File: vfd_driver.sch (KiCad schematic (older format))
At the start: 29 parts, among them J1 Input, J2 FIL, J3 HV, Q1 IRLZ34, U1 LM4871, U8 LM555

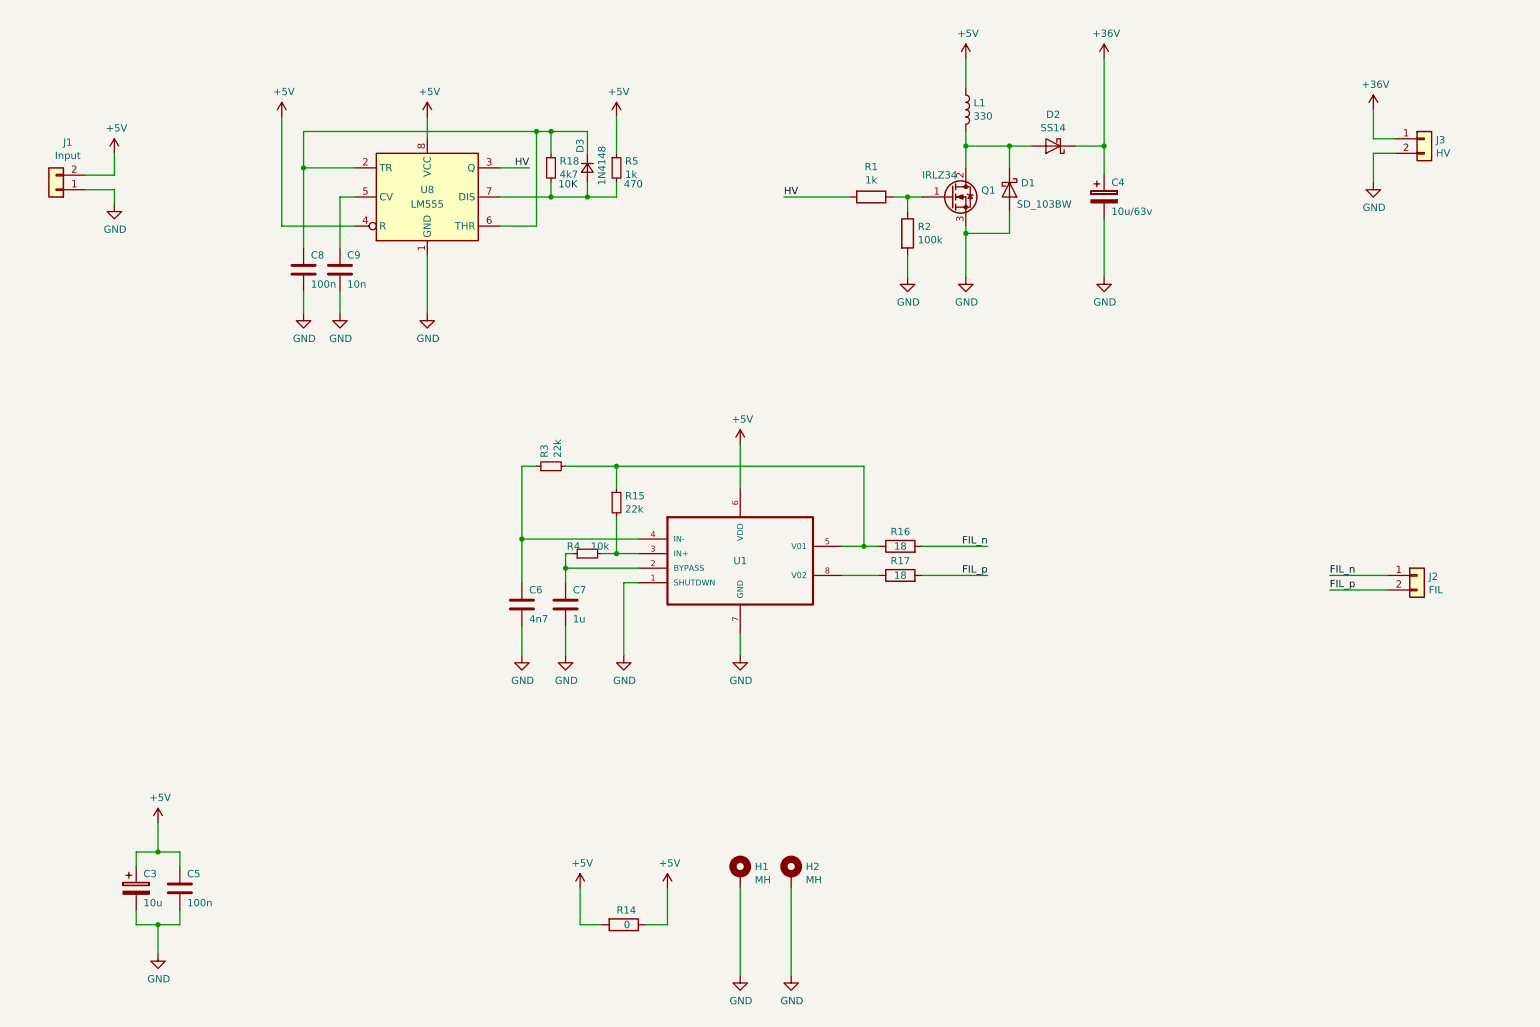
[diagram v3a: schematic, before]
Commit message: Separated input for the step up driver so ca be supply with 12V.
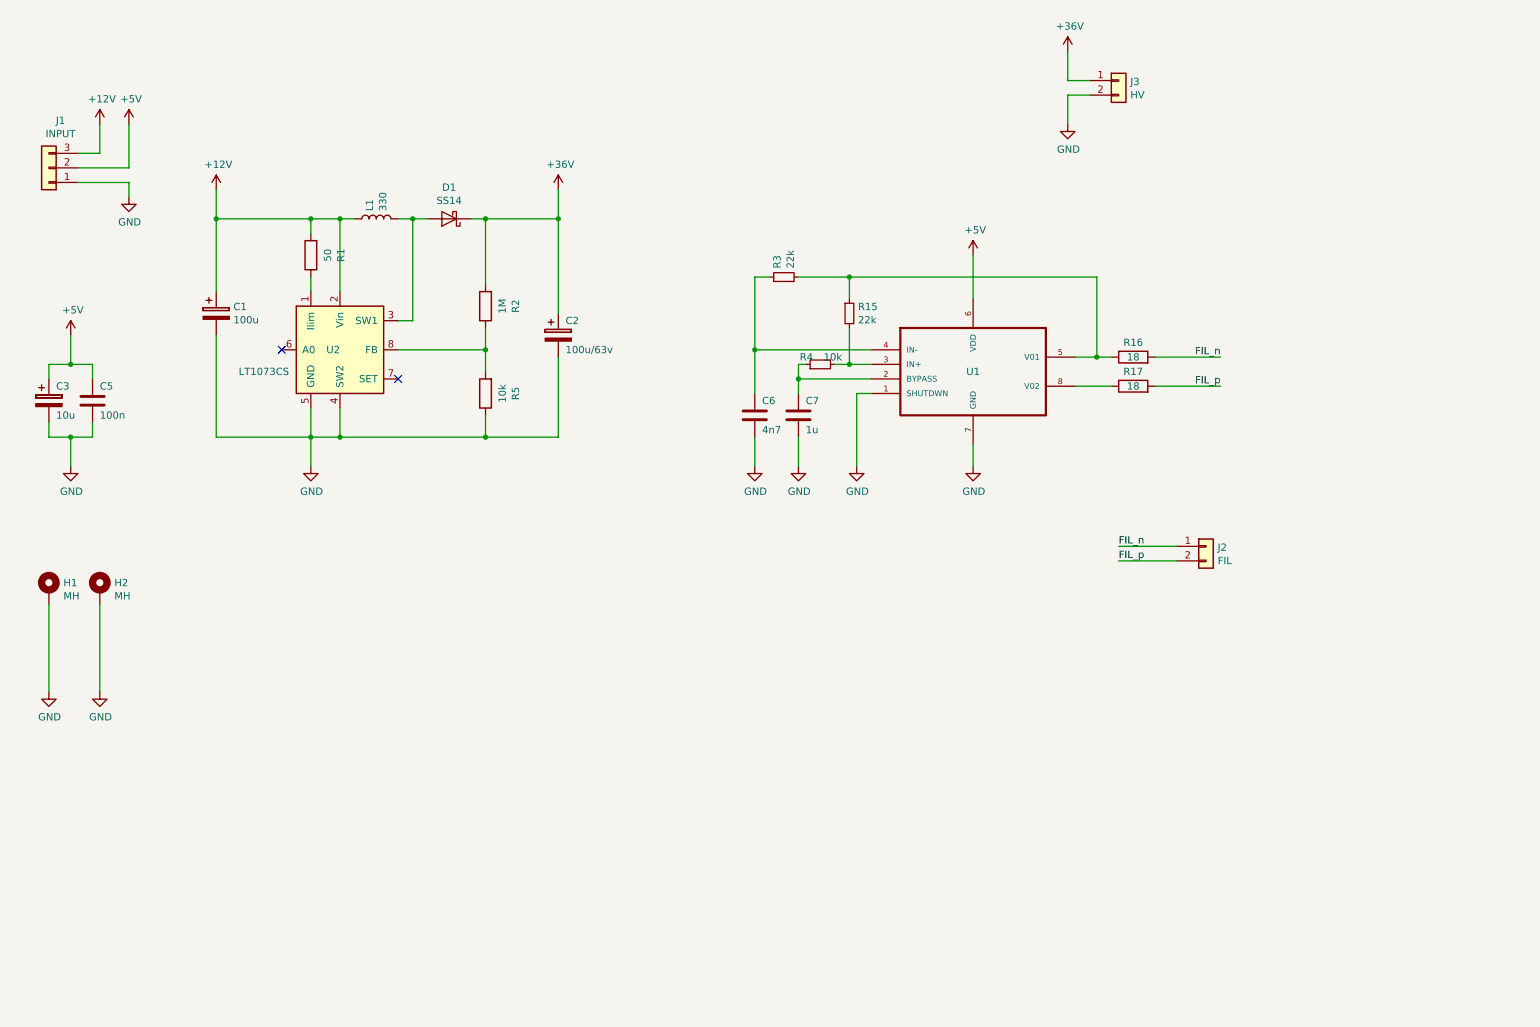
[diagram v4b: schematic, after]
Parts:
- removed C4: 10u/63v, Capacitor_THT:CP_Radial_D8.0mm_P5.00mm, symbol Device:CP
- removed C8: 100n, Capacitor_THT:C_Rect_L7.0mm_W2.0mm_P5.00mm, symbol Device:C
- removed C9: 10n, Capacitor_SMD:C_0805_2012Metric_Pad1.15x1.40mm_HandSolder, symbol Device:C
- removed D2: SS14, Diode_SMD:D_SMA_Handsoldering, symbol Device:D_Schottky
- removed D3: 1N4148, Diode_SMD:D_MiniMELF, symbol Device:D_Small
- removed J1: Input, Connector_PinHeader_2.54mm:PinHeader_1x02_P2.54mm_Vertical, symbol Connector_Generic:Conn_01x02
- removed Q1: IRLZ34, Package_TO_SOT_THT:TO-220-3_Vertical, symbol Device:Q_NMOS_GDS
- removed R14: 0, Resistor_SMD:R_1206_3216Metric, symbol Device:R
- removed R18: 4k7, Resistor_SMD:R_0805_2012Metric_Pad1.15x1.40mm_HandSolder, symbol Device:R_Small
- removed R5: 1k, Resistor_SMD:R_0805_2012Metric_Pad1.15x1.40mm_HandSolder, symbol Device:R_Small
- removed U8: LM555, Package_DIP:DIP-8_W7.62mm_Socket_LongPads, symbol Timer:LM555
- added C1: 100u, Capacitor_Tantalum_SMD:CP_EIA-7343-15_Kemet-W_Pad2.25x2.55mm_HandSolder, symbol Device:CP
- added C2: 100u/63v, Capacitor_THT:CP_Radial_D8.0mm_P5.00mm, symbol Device:CP
- added J1: INPUT, Connector_PinHeader_2.54mm:PinHeader_1x03_P2.54mm_Vertical, symbol Connector_Generic:Conn_01x03
- added R5: 10k, Resistor_SMD:R_0805_2012Metric_Pad1.15x1.40mm_HandSolder, symbol Device:R
- added U2: LT1073CS, Package_SO:SOIC-8_3.9x4.9mm_P1.27mm, symbol Regulator_Switching:LT1073CS
- D1: value SD_103BW -> SS14; footprint Diode_SMD:D_SOD-123 -> Diode_SMD:D_SMA_Handsoldering
- R1: value 1k -> 50
- R2: value 100k -> 1M
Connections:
- net +36V: now also D1.1 (K), R2.2, C2.1
- net +5V: now also J1.2 (Pin_2); no longer L1.1
- net GND: now also C1.2, C2.2, J1.1 (Pin_1), R5.1, U2.4 (SW2), U2.5 (GND); no longer D1.2 (A), R2.2
- net at R1.1: now also U2.1 (Ilim); no longer R2.1
- net at L1.2: now also D1.2 (A), U2.3 (SW1); no longer D1.1 (K)
- net HV renamed +12V
- net +12V: now also L1.1, C1.1, J1.3 (Pin_3), U2.2 (Vin)
- new net: R2.1, R5.2, U2.8 (FB)
- no-connect marks 0 -> 2
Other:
- note removed: "10K"
- note removed: "470"
- moved on the sheet: C3, C5, C6, C7, H1, H2, J2, J3, R15, R16, R17, R3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

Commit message: rescue parts
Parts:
- U1: symbol vfd_driver-rescue:LM4871-LM4871 -> vfd_driver-rescue:LM4871-LM4871-vfd_driver-rescue
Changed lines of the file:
@@
 	1100 3600 1100 3800
 $Comp
-L vfd_driver-rescue:LM4871-LM4871 U1
+L vfd_driver-rescue:LM4871-LM4871-vfd_driver-rescue U1
 U 1 1 5C9EEB87
 P 7300 3150
